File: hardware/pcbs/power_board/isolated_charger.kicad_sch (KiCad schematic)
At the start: 12 parts, among them J4 USB_A, U1 VRB1205S-6WR3, U2 LTV-247, U3 NCP380

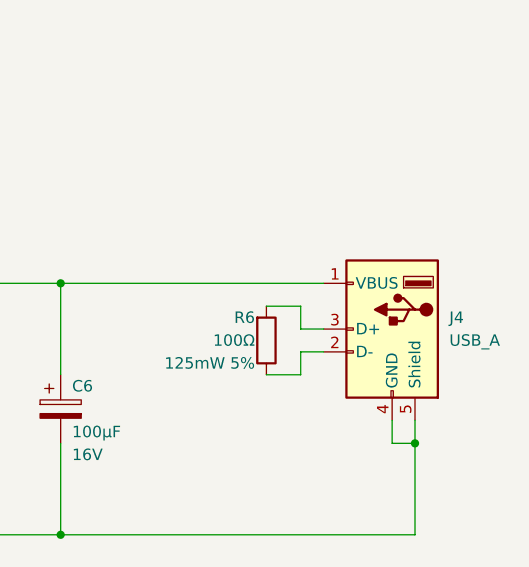
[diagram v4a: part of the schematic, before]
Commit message: power_board: arrange front panel components
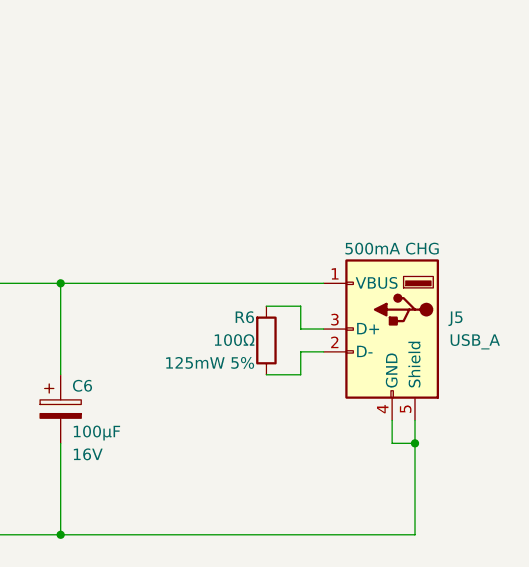
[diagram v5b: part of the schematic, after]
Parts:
- J5: renamed from J4; Purpose (none) -> 500mA CHG
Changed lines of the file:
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@@
   (symbol (lib_id "power:GND") (at 67.31 114.3 0) (unit 1)
     (in_bom yes) (on_board yes) (dnp no) (fields_autoplaced)
-    (property "Reference" "#PWR018" (at 67.31 120.65 0)
+    (property "Reference" "#PWR019" (at 67.31 120.65 0)
       (effects (font (size 1.27 1.27)) hide)
     )
@@
       (project "power_board"
         (path "/4b166175-80a4-48c6-994d-6e62a6160b87/2e2b9578-5dbd-4b2d-88fb-256ac9c8dd75/bdb69c9c-123a-4faa-b5c1-7130aac5ebc2"
-          (reference "#PWR018") (unit 1)
-        )
-        (path "/4b166175-80a4-48c6-994d-6e62a6160b87/2e2b9578-5dbd-4b2d-88fb-256ac9c8dd75/6373063e-1125-40d9-b0ec-3e2cb2886aea"
-          (reference "#PWR015") (unit 1)
-        )
-        (path "/4b166175-80a4-48c6-994d-6e62a6160b87/2e2b9578-5dbd-4b2d-88fb-256ac9c8dd75/32f9baea-32bc-4a84-b83a-18c67cc6248e"
-          (reference "#PWR09") (unit 1)
-        )
-        (path "/4b166175-80a4-48c6-994d-6e62a6160b87/2e2b9578-5dbd-4b2d-88fb-256ac9c8dd75/5f362cd5-d351-4250-994a-9f336837035c"
-          (reference "#PWR012") (unit 1)
+          (reference "#PWR019") (unit 1)
+        )
+        (path "/4b166175-80a4-48c6-994d-6e62a6160b87/2e2b9578-5dbd-4b2d-88fb-256ac9c8dd75/6373063e-1125-40d9-b0ec-3e2cb2886aea"
+          (reference "#PWR016") (unit 1)
+        )
+        (path "/4b166175-80a4-48c6-994d-6e62a6160b87/2e2b9578-5dbd-4b2d-88fb-256ac9c8dd75/32f9baea-32bc-4a84-b83a-18c67cc6248e"
+          (reference "#PWR010") (unit 1)
+        )
+        (path "/4b166175-80a4-48c6-994d-6e62a6160b87/2e2b9578-5dbd-4b2d-88fb-256ac9c8dd75/5f362cd5-d351-4250-994a-9f336837035c"
+          (reference "#PWR013") (unit 1)
         )
       )
@@
   )
   (symbol (lib_id "Connector:USB_A") (at 255.27 93.98 0) (mirror y) (unit 1)
-    (in_bom yes) (on_board yes) (dnp no) (fields_autoplaced)
-    (property "Reference" "J4" (at 261.62 92.71 0)
+    (in_bom yes) (on_board yes) (dnp no)
+    (property "Reference" "J5" (at 261.62 92.71 0)
       (effects (font (size 1.27 1.27)) (justify right))
     )
@@
     (property "Shop" "https://eu.mouser.com/ProductDetail/Amphenol-Commercial-Products/UE27AC5410H?qs=JOekRM69xWp%2FpXBIdMB8qQ%3D%3D" (at 255.27 93.98 0)
       (effects (font (size 1.27 1.27)) hide)
+    )
+    (property "Purpose" "500mA CHG" (at 255.27 85.09 0)
+      (effects (font (size 1.27 1.27)))
     )
     (pin "1")
@@
       (project "power_board"
         (path "/4b166175-80a4-48c6-994d-6e62a6160b87/2e2b9578-5dbd-4b2d-88fb-256ac9c8dd75/32f9baea-32bc-4a84-b83a-18c67cc6248e"
-          (reference "J4") (unit 1)
-        )
-        (path "/4b166175-80a4-48c6-994d-6e62a6160b87/2e2b9578-5dbd-4b2d-88fb-256ac9c8dd75/5f362cd5-d351-4250-994a-9f336837035c"
           (reference "J5") (unit 1)
         )
-        (path "/4b166175-80a4-48c6-994d-6e62a6160b87/2e2b9578-5dbd-4b2d-88fb-256ac9c8dd75/6373063e-1125-40d9-b0ec-3e2cb2886aea"
+        (path "/4b166175-80a4-48c6-994d-6e62a6160b87/2e2b9578-5dbd-4b2d-88fb-256ac9c8dd75/5f362cd5-d351-4250-994a-9f336837035c"
           (reference "J6") (unit 1)
         )
-        (path "/4b166175-80a4-48c6-994d-6e62a6160b87/2e2b9578-5dbd-4b2d-88fb-256ac9c8dd75/bdb69c9c-123a-4faa-b5c1-7130aac5ebc2"
+        (path "/4b166175-80a4-48c6-994d-6e62a6160b87/2e2b9578-5dbd-4b2d-88fb-256ac9c8dd75/6373063e-1125-40d9-b0ec-3e2cb2886aea"
           (reference "J7") (unit 1)
+        )
+        (path "/4b166175-80a4-48c6-994d-6e62a6160b87/2e2b9578-5dbd-4b2d-88fb-256ac9c8dd75/bdb69c9c-123a-4faa-b5c1-7130aac5ebc2"
+          (reference "J8") (unit 1)
         )
       )
@@
   (symbol (lib_id "power:GND") (at 172.72 72.39 90) (unit 1)
     (in_bom yes) (on_board yes) (dnp no) (fields_autoplaced)
-    (property "Reference" "#PWR020" (at 179.07 72.39 0)
+    (property "Reference" "#PWR021" (at 179.07 72.39 0)
       (effects (font (size 1.27 1.27)) hide)
     )
@@
       (project "power_board"
         (path "/4b166175-80a4-48c6-994d-6e62a6160b87/2e2b9578-5dbd-4b2d-88fb-256ac9c8dd75/bdb69c9c-123a-4faa-b5c1-7130aac5ebc2"
-          (reference "#PWR020") (unit 1)
-        )
-        (path "/4b166175-80a4-48c6-994d-6e62a6160b87/2e2b9578-5dbd-4b2d-88fb-256ac9c8dd75/6373063e-1125-40d9-b0ec-3e2cb2886aea"
-          (reference "#PWR017") (unit 1)
-        )
-        (path "/4b166175-80a4-48c6-994d-6e62a6160b87/2e2b9578-5dbd-4b2d-88fb-256ac9c8dd75/32f9baea-32bc-4a84-b83a-18c67cc6248e"
-          (reference "#PWR011") (unit 1)
-        )
-        (path "/4b166175-80a4-48c6-994d-6e62a6160b87/2e2b9578-5dbd-4b2d-88fb-256ac9c8dd75/5f362cd5-d351-4250-994a-9f336837035c"
-          (reference "#PWR014") (unit 1)
+          (reference "#PWR021") (unit 1)
+        )
+        (path "/4b166175-80a4-48c6-994d-6e62a6160b87/2e2b9578-5dbd-4b2d-88fb-256ac9c8dd75/6373063e-1125-40d9-b0ec-3e2cb2886aea"
+          (reference "#PWR018") (unit 1)
+        )
+        (path "/4b166175-80a4-48c6-994d-6e62a6160b87/2e2b9578-5dbd-4b2d-88fb-256ac9c8dd75/32f9baea-32bc-4a84-b83a-18c67cc6248e"
+          (reference "#PWR012") (unit 1)
+        )
+        (path "/4b166175-80a4-48c6-994d-6e62a6160b87/2e2b9578-5dbd-4b2d-88fb-256ac9c8dd75/5f362cd5-d351-4250-994a-9f336837035c"
+          (reference "#PWR015") (unit 1)
         )
       )
@@
   (symbol (lib_id "power:GND") (at 78.74 114.3 0) (unit 1)
     (in_bom yes) (on_board yes) (dnp no) (fields_autoplaced)
-    (property "Reference" "#PWR019" (at 78.74 120.65 0)
+    (property "Reference" "#PWR020" (at 78.74 120.65 0)
       (effects (font (size 1.27 1.27)) hide)
     )
@@
       (project "power_board"
         (path "/4b166175-80a4-48c6-994d-6e62a6160b87/2e2b9578-5dbd-4b2d-88fb-256ac9c8dd75/bdb69c9c-123a-4faa-b5c1-7130aac5ebc2"
-          (reference "#PWR019") (unit 1)
-        )
-        (path "/4b166175-80a4-48c6-994d-6e62a6160b87/2e2b9578-5dbd-4b2d-88fb-256ac9c8dd75/6373063e-1125-40d9-b0ec-3e2cb2886aea"
-          (reference "#PWR016") (unit 1)
-        )
-        (path "/4b166175-80a4-48c6-994d-6e62a6160b87/2e2b9578-5dbd-4b2d-88fb-256ac9c8dd75/32f9baea-32bc-4a84-b83a-18c67cc6248e"
-          (reference "#PWR010") (unit 1)
-        )
-        (path "/4b166175-80a4-48c6-994d-6e62a6160b87/2e2b9578-5dbd-4b2d-88fb-256ac9c8dd75/5f362cd5-d351-4250-994a-9f336837035c"
-          (reference "#PWR013") (unit 1)
-        )
-      )
+          (reference "#PWR020") (unit 1)
+        )
+        (path "/4b166175-80a4-48c6-994d-6e62a6160b87/2e2b9578-5dbd-4b2d-88fb-256ac9c8dd75/6373063e-1125-40d9-b0ec-3e2cb2886aea"
+          (reference "#PWR017") (unit 1)
+        )
+        (path "/4b166175-80a4-48c6-994d-6e62a6160b87/2e2b9578-5dbd-4b2d-88fb-256ac9c8dd75/32f9baea-32bc-4a84-b83a-18c67cc6248e"
+          (reference "#PWR011") (unit 1)
+        )
+        (path "/4b166175-80a4-48c6-994d-6e62a6160b87/2e2b9578-5dbd-4b2d-88fb-256ac9c8dd75/5f362cd5-d351-4250-994a-9f336837035c"
+          (reference "#PWR014") (unit 1)
+        )
+      )

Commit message: power_board: update caps
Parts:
- C6: footprint Capacitor_SMD:CP_Elec_6.3x5.4 -> Capacitor_THT:CP_Radial_D5.0mm_P2.00mm; Shop https://store.comet.bg/Catalogue/Product/29563/ -> https://store.comet.bg/Catalogue/Product/3785/
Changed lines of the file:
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@@
       (effects (font (size 1.27 1.27)) (justify left))
     )
-    (property "Footprint" "Capacitor_SMD:CP_Elec_6.3x5.4" (at 219.4052 106.68 0)
+    (property "Footprint" "Capacitor_THT:CP_Radial_D5.0mm_P2.00mm" (at 219.4052 106.68 0)
       (effects (font (size 1.27 1.27)) hide)
     )
@@
       (effects (font (size 1.27 1.27)) hide)
     )
-    (property "Shop" "https://store.comet.bg/Catalogue/Product/29563/" (at 218.44 102.87 0)
+    (property "Shop" "https://store.comet.bg/Catalogue/Product/3785/" (at 218.44 102.87 0)
       (effects (font (size 1.27 1.27)) hide)
     )

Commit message: use a sideways usb connector for USB-3
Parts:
- J5: footprint conn:USB_A_Amphenol_UE27AC5410H -> conn:USB_A_Amphenol_GSB19111KEU; Shop https://eu.mouser.com/ProductDetail/Amphenol-Commercial-Products/UE27AC5410H?qs=JOekRM69xWp%2FpXBIdMB8qQ%3D%3D -> https://eu.mouser.com/ProductDetail/Amphenol-Commercial-Products/GSB19111KEU?qs=f9yNj16SXrIKY3kSdPAsqw%3D%3D

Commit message: power_board: add power cycler
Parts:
- C6: footprint Capacitor_THT:CP_Radial_D5.0mm_P2.00mm -> Capacitor_SMD:CP_Elec_6.3x5.4; Shop https://store.comet.bg/Catalogue/Product/3785/ -> https://store.comet.bg/Catalogue/Product/29563/
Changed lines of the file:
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@@
 			)
 		)
-		(property "Footprint" "Capacitor_THT:CP_Radial_D5.0mm_P2.00mm"
+		(property "Footprint" "Capacitor_SMD:CP_Elec_6.3x5.4"
 			(at 219.4052 106.68 0)
 			(effects
@@
 			)
 		)
-		(property "Shop" "https://store.comet.bg/Catalogue/Product/3785/"
+		(property "Shop" "https://store.comet.bg/Catalogue/Product/29563/"
 			(at 218.44 102.87 0)
 			(effects
